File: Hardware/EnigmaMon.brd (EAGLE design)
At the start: 100 x 80 mm, 34 parts, among them T1 BC548, T2 BC548, T3 BC548, T4 BC548, T5 BC548, T6 BC548

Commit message: Added some interesting muxers
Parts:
- removed ARD2: ARD_DIGITAL_1, EnigmaMon:ARD_DIGITAL_1
- removed JP1: (no value), pinhead:2X06
- removed JP2: (no value), pinhead:1X05
- added C2: 10uF, rcl:C025-025X050
- added D8, D9: 1N4004, diode:DO41-10
- added FAN7, FAN8: (no value), pinhead:1X03
- added IC1: 4051N, 40xx:DIL16
- added IC2: TLC5940, EnigmaMon:DIL28-3
- added R15, R17: 1k, rcl:0204/7
- added R16, R18, R_BLANK: 10k, rcl:0204/7
- added R_IREF: 2.2k, rcl:0204/7
- added T8, T9: BC548, transistor:TO92
- added U$1: ARD_POWER, EnigmaMon:ARD_POWER
- added U$2: ARD_DIGITAL_1, EnigmaMon:ARD_DIGITAL_1
- added U$3: ARD_DIGITAL_2, EnigmaMon:ARD_DIGITAL_2
- R1, R4: value (none) -> 10k; device rcl:0204/7 -> rcl:0207/10
- R10, R12, R6, R8: value (none) -> 10k
- R11, R2, R3, R5, R7, R9: value (none) -> 1k
- moved R12 67.3 mm to (71.1, 71.1), turned to 90 degrees
- moved FAN6 60.2 mm to (71.1, 59.7), turned to 270 degrees
- moved R10 57.5 mm to (66.0, 71.1), turned to 90 degrees
- moved FAN5 53.9 mm to (66.0, 59.7), turned to 270 degrees
- moved FAN1 50.9 mm to (45.7, 59.7), turned to 270 degrees
- moved FAN4 49.4 mm to (61.0, 59.7), turned to 270 degrees
- moved R8 48.4 mm to (61.0, 71.1), turned to 90 degrees
- moved FAN2 47.8 mm to (50.8, 59.7), turned to 270 degrees
- moved FAN3 47.3 mm to (55.9, 59.7), turned to 270 degrees
- moved T1 46.6 mm to (41.9, 38.1), turned to 0 degrees
- moved R6 40.4 mm to (55.9, 71.1), turned to 90 degrees
- moved R2 39.7 mm to (41.9, 31.8), turned to 90 degrees
- moved D6 39.4 mm to (73.7, 48.3), turned to 270 degrees
- moved T2 37.0 mm to (48.3, 38.1), turned to 0 degrees
- moved R4 33.3 mm to (50.8, 69.8), turned to 90 degrees
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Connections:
- removed net +5V: JP2.4, R1.2, R10.2, R12.2, R4.2, R6.2, R8.2
- removed net 3.3V: JP2.5
- removed net LCD_DATA: ARD2.3
- new net FAN7_GND: D8.C, FAN7.3, T8.3
- new net FAN7_PWM: IC2.2, R15.1
- new net FAN7_TACHO: FAN7.1, IC1.15, R16.1
- new net FAN8_GND: D9.C, FAN8.3, T9.3
- new net FAN8_PWM: IC2.1, R17.1
- new net FAN8_TACHO: FAN8.1, IC1.1, R18.1
- new net FAN_TACHO: IC1.3, U$3.10
- new net N$10: IC2.20, R_IREF.1
- new net N$8: R15.2, T8.2
- new net N$9: R17.2, T9.2
- new net PWM_BLANK: IC2.23, R_BLANK.2, U$2.4
- new net PWM_GSCLK: IC2.18, U$2.5
- new net PWM_SCLK: IC2.25, U$2.7
- new net PWM_SIN: IC2.26, U$3.8
- new net PWM_VPRG: IC2.27, U$3.9
- new net PWM_XLAT: IC2.24, U$2.6
- new net TACHO_SEL0: IC1.11, U$3.11
- new net TACHO_SEL1: IC1.10, U$3.12
- new net TACHO_SEL2: IC1.9, U$3.13
- new net VCC: C2.1, IC1.16, IC2.19, IC2.21, R1.2, R10.2, R12.2, R16.2, R18.2, R4.2, R6.2, R8.2, R_BLANK.1, U$1.5V
- new net VEE: IC1.7
- net +12V: now also FAN7.2, FAN8.2, U$1.VIN; no longer JP2.1
- net FAN1_PWM: now also IC2.8; no longer JP1.2
- net FAN1_TACHO: now also IC1.12; no longer JP1.1
- net FAN2_PWM: now also IC2.7; no longer JP1.4
- net FAN2_TACHO: now also IC1.5; no longer JP1.3
- net FAN3_PWM: now also IC2.6; no longer JP1.6
- net FAN3_TACHO: now also IC1.13; no longer JP1.5
- net FAN4_PWM: now also IC2.5; no longer JP1.8
- net FAN4_TACHO: now also IC1.4; no longer JP1.7
- net FAN5_PWM: now also IC2.4; no longer JP1.10
- net FAN5_TACHO: now also IC1.14; no longer JP1.9
- net FAN6_PWM: now also IC2.3; no longer JP1.12
- net FAN6_TACHO: now also IC1.2; no longer JP1.11
- net GND: now also C2.2, D8.A, D9.A, IC1.6, IC1.8, IC2.22, R_IREF.2, T8.1, T9.1, U$1.GND@1, U$1.GND@2, U$3.GND; no longer JP2.2, JP2.3
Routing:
- net VCC: track 0.00 -> 227.1 mm
- net GND: track 140.7 -> 331.0 mm, vias 6 -> 0
- net +5V: track 101.6 -> 0.00 mm, vias 7 -> 0
- net PWM_VPRG: track 0.00 -> 72.7 mm
- net PWM_BLANK: track 0.00 -> 72.5 mm, vias 0 -> 2
- net PWM_SIN: track 0.00 -> 67.6 mm
- net FAN8_TACHO: track 0.00 -> 67.1 mm
- net PWM_SCLK: track 0.00 -> 67.1 mm, vias 0 -> 2
- net PWM_XLAT: track 0.00 -> 65.8 mm, vias 0 -> 2
- net FAN6_PWM: track 71.1 -> 11.2 mm
- net FAN_TACHO: track 0.00 -> 56.9 mm
- net FAN5_TACHO: track 93.8 -> 39.9 mm
- net FAN6_TACHO: track 107.2 -> 54.4 mm
- net FAN7_TACHO: track 0.00 -> 52.6 mm
- net PWM_GSCLK: track 0.00 -> 51.1 mm
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
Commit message: Added some interesting muxers
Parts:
- PWR: device EnigmaMon:PIN02-1 -> EnigmaMon:1X02
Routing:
- net GND: track 331.0 -> 332.3 mm
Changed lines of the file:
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@@
 </autorouter>
 <elements>
-<element name="PWR" library="EnigmaMon" package="PIN02-1" value="" x="91.44" y="59.69" rot="R90"/>
+<element name="PWR" library="EnigmaMon" package="1X02" value="" x="91.44" y="59.69" rot="R90"/>
 <element name="FAN1" library="pinhead" package="1X03" value="" x="45.72" y="59.69" rot="R270"/>
 <element name="T1" library="transistor" package="TO92" value="BC548" x="41.91" y="38.1" smashed="yes">
@@
 <wire x1="71.12" y1="59.69" x2="76.2" y2="59.69" width="0.8128" layer="16"/>
 <wire x1="71.12" y1="59.69" x2="81.28" y2="59.69" width="0.8128" layer="16"/>
-<wire x1="81.28" y1="59.69" x2="91.44" y2="59.69" width="0.8128" layer="16"/>
+<wire x1="81.28" y1="59.69" x2="91.44" y2="60.96" width="0.8128" layer="16"/>
 </signal>
 <signal name="GND">
@@
 <wire x1="35.56" y1="49.53" x2="8.89" y2="49.53" width="0.8128" layer="16"/>
 <wire x1="8.89" y1="49.53" x2="8.89" y2="62.23" width="0.8128" layer="16"/>
-<wire x1="91.44" y1="57.15" x2="91.44" y2="43.18" width="0.8128" layer="16"/>
+<wire x1="91.44" y1="58.42" x2="91.44" y2="43.18" width="0.8128" layer="16"/>
 <wire x1="91.44" y1="43.18" x2="90.17" y2="41.91" width="0.8128" layer="16"/>
 <wire x1="90.17" y1="41.91" x2="87.63" y2="41.91" width="0.8128" layer="16"/>

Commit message: Added VMR
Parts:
- added C1, C3: 10uF, rcl:E2,5-6
- added INPUT_PWR: (no value), EnigmaMon:1X02
- added LM7805: (no value), EnigmaMon:78XXL
- added R13, R14: 220, rcl:0204/7
- added U$4: DTS6, EnigmaMon:DTS6
- PWR: device EnigmaMon:1X02 -> EnigmaMon:LED3MM
- moved PWR 72.6 mm to (19.1, 54.6), turned to 270 degrees
- moved R4 5.24 mm to (55.9, 71.1)
- moved D1 5.24 mm to (47.0, 49.5)
- moved D2 5.24 mm to (53.3, 49.5)
- moved D4 5.24 mm to (66.0, 49.5)
- moved FAN2 5.24 mm to (55.9, 61.0)
- moved FAN4 5.24 mm to (66.0, 61.0)
- moved R2 5.24 mm to (47.0, 33.0)
- moved R3 5.24 mm to (53.3, 33.0)
- moved R7 5.24 mm to (66.0, 33.0)
- moved R8 5.24 mm to (66.0, 72.4)
- moved T1 5.24 mm to (47.0, 39.4)
- moved T2 5.24 mm to (53.3, 39.4)
- moved T4 5.24 mm to (66.0, 39.4)
- moved R1 5.24 mm to (50.8, 71.1)
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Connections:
- new net N$12: R14.2, U$4.3, U$4.4
- new net N$7: PWR.K, R13.2
- new net RESET: R14.1, U$1.RESET
- net +12V: now also C1.+, INPUT_PWR.2, LM7805.IN; no longer PWR.2
- net GND: now also C1.-, C3.-, INPUT_PWR.1, LM7805.GND, R13.1, U$4.1, U$4.2; no longer PWR.1
- net VCC: now also C3.+, LM7805.OUT, PWR.A
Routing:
- net GND: track 332.3 -> 363.5 mm
- net VCC: track 227.1 -> 258.1 mm, vias 0 -> 2
- net N$12: track 0.00 -> 25.9 mm
- net +12V: track 98.2 -> 111.9 mm
- net PWM_VPRG: track 72.7 -> 80.3 mm
- net TACHO_SEL2: track 38.1 -> 45.7 mm
- net TACHO_SEL1: track 47.5 -> 55.1 mm
- net TACHO_SEL0: track 47.5 -> 55.1 mm
- net PWM_SCLK: track 67.1 -> 74.7 mm
- net PWM_GSCLK: track 51.1 -> 58.7 mm
- net PWM_XLAT: track 65.8 -> 73.4 mm
- net PWM_SIN: track 67.6 -> 75.2 mm
- net PWM_BLANK: track 72.5 -> 80.1 mm
- net FAN_TACHO: track 56.9 -> 63.1 mm
- net RESET: track 0.00 -> 5.61 mm
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
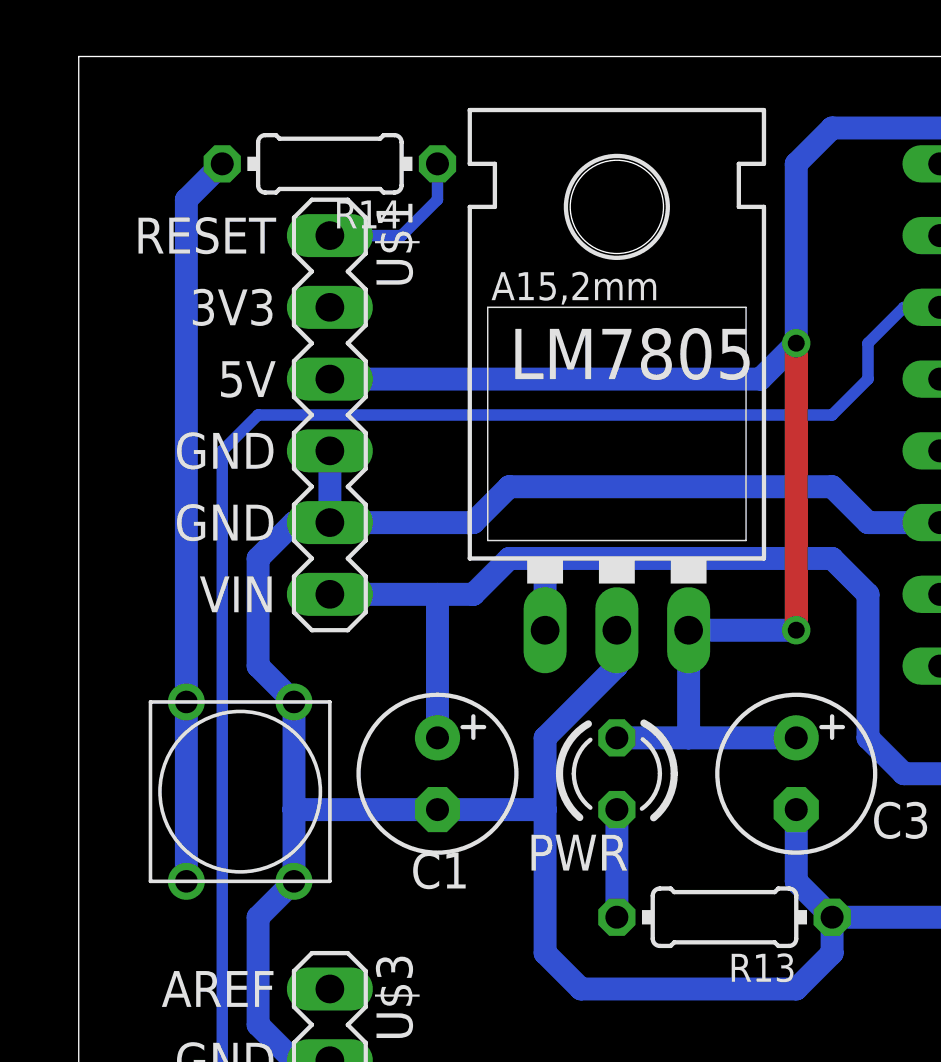
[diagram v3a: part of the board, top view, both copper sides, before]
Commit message: Fixed error with reset switch
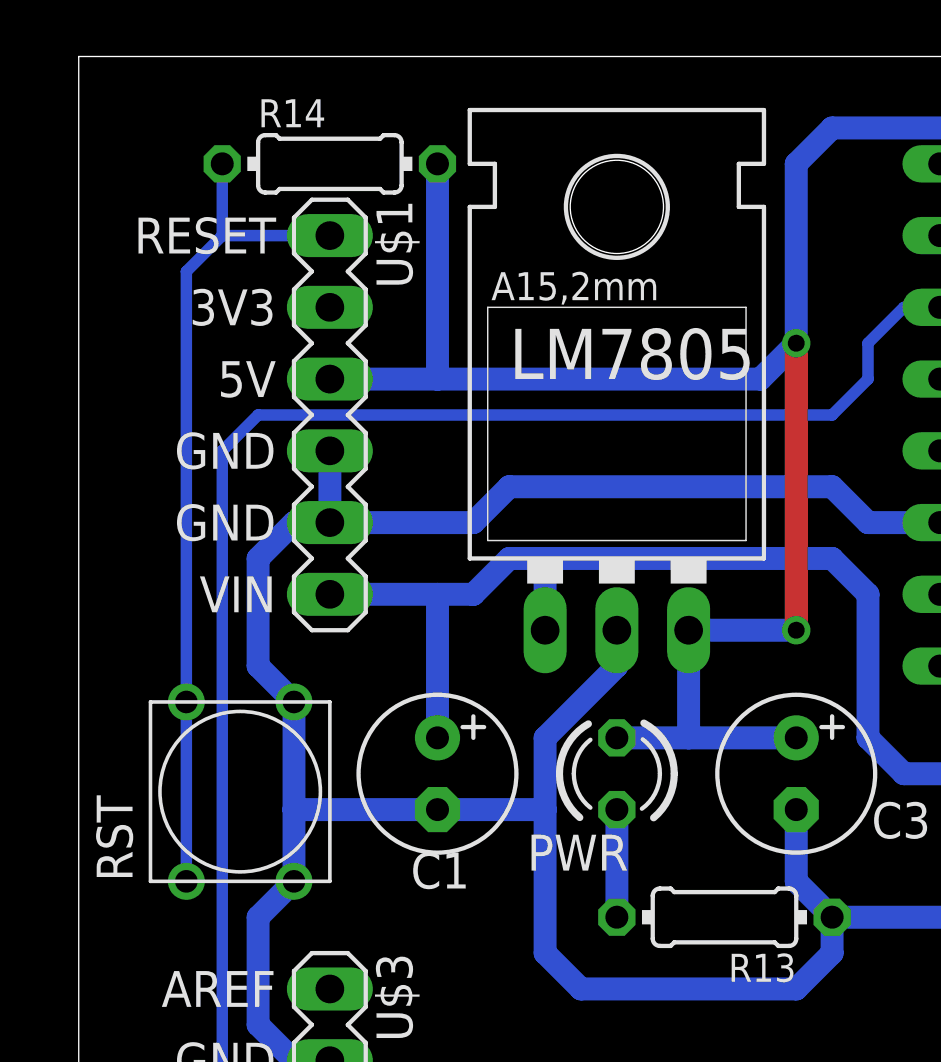
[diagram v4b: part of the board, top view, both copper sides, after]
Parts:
- removed U$4: DTS6, EnigmaMon:DTS6
- added RST: DTS6, EnigmaMon:DTS6
- turned R14 to 0 degrees
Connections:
- removed net N$12: R14.2, U$4.3, U$4.4
- net GND: now also RST.3, RST.4; no longer U$4.1, U$4.2
- net RESET: now also RST.1, RST.2
- net VCC: now also R14.2
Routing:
- net N$12: track 25.9 -> 0.00 mm
- net RESET: track 5.61 -> 29.7 mm
- net VCC: track 258.1 -> 265.7 mm
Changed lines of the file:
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@@
 </element>
 <element name="R13" library="rcl" package="0204/7" value="220" x="22.86" y="49.53" rot="R180"/>
-<element name="R14" library="rcl" package="0204/7" value="220" x="8.89" y="76.2" rot="R180"/>
-<element name="U$4" library="EnigmaMon" package="DTS6" value="DTS6" x="5.08" y="54.61" rot="R270"/>
+<element name="R14" library="rcl" package="0204/7" value="220" x="8.89" y="76.2"/>
+<element name="RST" library="EnigmaMon" package="DTS6" value="DTS6" x="6.35" y="53.34" rot="R90"/>
 </elements>
 <signals>
@@
 <wire x1="16.51" y1="48.26" x2="16.51" y2="53.34" width="0.8128" layer="16"/>
 <wire x1="12.7" y1="53.34" x2="7.62" y2="53.34" width="0.8128" layer="16"/>
-<wire x1="7.62" y1="53.34" x2="7.62" y2="57.15" width="0.8128" layer="16"/>
 <wire x1="7.62" y1="57.15" x2="6.35" y2="58.42" width="0.8128" layer="16"/>
 <wire x1="6.35" y1="58.42" x2="6.35" y2="62.23" width="0.8128" layer="16"/>
@@
 <contactref element="IC2" pad="22"/>
 <wire x1="72.39" y1="7.62" x2="72.39" y2="10.16" width="0.8128" layer="16"/>
-<wire x1="7.62" y1="53.34" x2="7.62" y2="50.8" width="0.8128" layer="16"/>
 <wire x1="7.62" y1="50.8" x2="6.35" y2="49.53" width="0.8128" layer="16"/>
 <wire x1="6.35" y1="49.53" x2="6.35" y2="45.72" width="0.8128" layer="16"/>
@@
 <wire x1="16.51" y1="55.88" x2="16.51" y2="53.34" width="0.8128" layer="16"/>
 <wire x1="16.51" y1="53.34" x2="12.7" y2="53.34" width="0.8128" layer="16"/>
-<contactref element="U$4" pad="1"/>
-<contactref element="U$4" pad="2"/>
+<contactref element="RST" pad="4"/>
+<contactref element="RST" pad="3"/>
+<wire x1="7.62" y1="57.15" x2="7.62" y2="53.34" width="0.8128" layer="16"/>
+<wire x1="7.62" y1="50.8" x2="7.62" y2="53.34" width="0.8128" layer="16"/>
 </signal>
 <signal name="FAN4_TACHO">
@@
 <contactref element="R10" pad="2"/>
 <contactref element="R12" pad="2"/>
-<wire x1="8.89" y1="68.58" x2="24.13" y2="68.58" width="0.8128" layer="16"/>
+<wire x1="8.89" y1="68.58" x2="12.7" y2="68.58" width="0.8128" layer="16"/>
+<wire x1="12.7" y1="68.58" x2="24.13" y2="68.58" width="0.8128" layer="16"/>
 <wire x1="25.4" y1="69.85" x2="25.4" y2="76.2" width="0.8128" layer="16"/>
 <wire x1="25.4" y1="76.2" x2="26.67" y2="77.47" width="0.8128" layer="16"/>
@@
 <via x="25.4" y="69.85" extent="1-16" drill="0.6" shape="square"/>
 <wire x1="25.4" y1="69.85" x2="24.13" y2="68.58" width="0.8128" layer="16"/>
+<contactref element="R14" pad="2"/>
+<wire x1="12.7" y1="76.2" x2="12.7" y2="68.58" width="0.8128" layer="16"/>
+<wire x1="12.7" y1="68.58" x2="8.89" y2="68.58" width="0" layer="19" extent="1-16"/>
 </signal>
 <signal name="TACHO_SEL2">
@@
 <wire x1="19.05" y1="53.34" x2="19.05" y2="49.53" width="0.8128" layer="16"/>
 </signal>
-<signal name="N$12">
-<contactref element="R14" pad="2"/>
-<contactref element="U$4" pad="3"/>
-<contactref element="U$4" pad="4"/>
-<wire x1="3.81" y1="50.8" x2="3.81" y2="57.15" width="0.8128" layer="16"/>
-<wire x1="3.81" y1="57.15" x2="3.81" y2="74.93" width="0.8128" layer="16"/>
-<wire x1="3.81" y1="74.93" x2="5.08" y2="76.2" width="0.8128" layer="16"/>
-</signal>
 <signal name="RESET">
 <contactref element="R14" pad="1"/>
 <contactref element="U$1" pad="RESET"/>
-<wire x1="12.7" y1="76.2" x2="12.7" y2="74.93" width="0.4064" layer="16"/>
-<wire x1="12.7" y1="74.93" x2="11.43" y2="73.66" width="0.4064" layer="16"/>
-<wire x1="11.43" y1="73.66" x2="8.89" y2="73.66" width="0.4064" layer="16"/>
+<wire x1="5.08" y1="76.2" x2="5.08" y2="73.66" width="0.4064" layer="16"/>
+<contactref element="RST" pad="1"/>
+<contactref element="RST" pad="2"/>
+<wire x1="3.81" y1="57.15" x2="3.81" y2="72.39" width="0.4064" layer="16"/>
+<wire x1="3.81" y1="72.39" x2="5.08" y2="73.66" width="0.4064" layer="16"/>
+<wire x1="5.08" y1="73.66" x2="8.89" y2="73.66" width="0.4064" layer="16"/>
+<wire x1="3.81" y1="57.15" x2="3.81" y2="50.8" width="0.4064" layer="16"/>
 </signal>
 </signals>

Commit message: Couple of minor updates
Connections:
- net GND: now also IC2.10, IC2.11, IC2.12, IC2.13, IC2.14, IC2.15, IC2.9
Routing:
- net GND: track 363.5 -> 394.5 mm
- net PWM_SIN: track 75.2 -> 89.0 mm
- net PWM_VPRG: track 80.3 -> 94.1 mm
- net PWM_XLAT: track 73.4 -> 77.0 mm
- net PWM_SCLK: track 74.7 -> 78.3 mm
- net PWM_GSCLK: track 58.7 -> 61.3 mm
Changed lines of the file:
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@@
 <wire x1="7.62" y1="57.15" x2="7.62" y2="53.34" width="0.8128" layer="16"/>
 <wire x1="7.62" y1="50.8" x2="7.62" y2="53.34" width="0.8128" layer="16"/>
+<contactref element="IC2" pad="9"/>
+<contactref element="IC2" pad="10"/>
+<contactref element="IC2" pad="11"/>
+<contactref element="IC2" pad="12"/>
+<contactref element="IC2" pad="13"/>
+<contactref element="IC2" pad="14"/>
+<contactref element="IC2" pad="15"/>
+<wire x1="44.45" y1="22.86" x2="43.18" y2="24.13" width="0.8128" layer="16"/>
+<wire x1="43.18" y1="24.13" x2="43.18" y2="33.02" width="0.8128" layer="16"/>
+<wire x1="44.45" y1="22.86" x2="46.99" y2="22.86" width="0.8128" layer="16"/>
+<wire x1="46.99" y1="22.86" x2="49.53" y2="22.86" width="0.8128" layer="16"/>
+<wire x1="49.53" y1="22.86" x2="52.07" y2="22.86" width="0.8128" layer="16"/>
+<wire x1="52.07" y1="22.86" x2="54.61" y2="22.86" width="0.8128" layer="16"/>
+<wire x1="54.61" y1="22.86" x2="57.15" y2="22.86" width="0.8128" layer="16"/>
+<wire x1="44.45" y1="22.86" x2="44.45" y2="15.24" width="0.8128" layer="16"/>
 </signal>
 <signal name="FAN4_TACHO">
@@
 <wire x1="8.89" y1="20.32" x2="22.86" y2="20.32" width="0.4064" layer="16"/>
 <wire x1="22.86" y1="20.32" x2="24.13" y2="19.05" width="0.4064" layer="16"/>
-<wire x1="24.13" y1="19.05" x2="24.13" y2="10.16" width="0.4064" layer="16"/>
-<wire x1="24.13" y1="10.16" x2="25.4" y2="8.89" width="0.4064" layer="16"/>
-<wire x1="25.4" y1="8.89" x2="50.8" y2="8.89" width="0.4064" layer="16"/>
-<wire x1="50.8" y1="8.89" x2="52.07" y2="10.16" width="0.4064" layer="16"/>
-<wire x1="52.07" y1="10.16" x2="52.07" y2="15.24" width="0.4064" layer="16"/>
+<wire x1="24.13" y1="19.05" x2="24.13" y2="8.89" width="0.4064" layer="16"/>
+<wire x1="24.13" y1="8.89" x2="25.4" y2="7.62" width="0.4064" layer="16"/>
+<wire x1="25.4" y1="7.62" x2="50.8" y2="7.62" width="0.4064" layer="16"/>
+<wire x1="50.8" y1="7.62" x2="52.07" y2="8.89" width="0.4064" layer="16"/>
+<wire x1="52.07" y1="8.89" x2="52.07" y2="15.24" width="0.4064" layer="16"/>
 </signal>
 <signal name="PWM_XLAT">
@@
 <wire x1="67.31" y1="15.24" x2="67.31" y2="11.43" width="0.4064" layer="16"/>
 <via x="67.31" y="11.43" extent="1-16" drill="0.6" shape="square"/>
-<wire x1="67.31" y1="11.43" x2="50.8" y2="11.43" width="0.4064" layer="1"/>
-<via x="50.8" y="11.43" extent="1-16" drill="0.6" shape="square"/>
-<wire x1="50.8" y1="11.43" x2="26.67" y2="11.43" width="0.4064" layer="16"/>
-<wire x1="26.67" y1="11.43" x2="25.4" y2="12.7" width="0.4064" layer="16"/>
-<wire x1="25.4" y1="12.7" x2="25.4" y2="21.59" width="0.4064" layer="16"/>
+<wire x1="67.31" y1="11.43" x2="55.88" y2="11.43" width="0.4064" layer="1"/>
+<wire x1="55.88" y1="11.43" x2="53.34" y2="8.89" width="0.4064" layer="1"/>
+<wire x1="53.34" y1="8.89" x2="49.53" y2="8.89" width="0.4064" layer="1"/>
+<via x="49.53" y="8.89" extent="1-16" drill="0.6" shape="square"/>
+<wire x1="49.53" y1="8.89" x2="26.67" y2="8.89" width="0.4064" layer="16"/>
+<wire x1="26.67" y1="8.89" x2="25.4" y2="10.16" width="0.4064" layer="16"/>
+<wire x1="25.4" y1="10.16" x2="25.4" y2="21.59" width="0.4064" layer="16"/>
 <wire x1="25.4" y1="21.59" x2="24.13" y2="22.86" width="0.4064" layer="16"/>
 <wire x1="24.13" y1="22.86" x2="8.89" y2="22.86" width="0.4064" layer="16"/>
@@
 <contactref element="IC2" pad="25"/>
 <contactref element="U$2" pad="7"/>
-<wire x1="50.8" y1="12.7" x2="27.94" y2="12.7" width="0.4064" layer="16"/>
-<wire x1="27.94" y1="12.7" x2="26.67" y2="13.97" width="0.4064" layer="16"/>
-<wire x1="26.67" y1="13.97" x2="26.67" y2="24.13" width="0.4064" layer="16"/>
+<wire x1="49.53" y1="10.16" x2="27.94" y2="10.16" width="0.4064" layer="16"/>
+<wire x1="27.94" y1="10.16" x2="26.67" y2="11.43" width="0.4064" layer="16"/>
+<wire x1="26.67" y1="11.43" x2="26.67" y2="24.13" width="0.4064" layer="16"/>
 <wire x1="26.67" y1="24.13" x2="25.4" y2="25.4" width="0.4064" layer="16"/>
 <wire x1="25.4" y1="25.4" x2="8.89" y2="25.4" width="0.4064" layer="16"/>
 <wire x1="69.85" y1="15.24" x2="69.85" y2="12.7" width="0.4064" layer="16"/>
 <via x="69.85" y="12.7" extent="1-16" drill="0.6" shape="square"/>
-<wire x1="69.85" y1="12.7" x2="50.8" y2="12.7" width="0.4064" layer="1"/>
-<via x="50.8" y="12.7" extent="1-16" drill="0.6" shape="square"/>
+<wire x1="69.85" y1="12.7" x2="55.88" y2="12.7" width="0.4064" layer="1"/>
+<wire x1="55.88" y1="12.7" x2="53.34" y2="10.16" width="0.4064" layer="1"/>
+<wire x1="53.34" y1="10.16" x2="49.53" y2="10.16" width="0.4064" layer="1"/>
+<via x="49.53" y="10.16" extent="1-16" drill="0.6" shape="square"/>
 </signal>
 <signal name="PWM_SIN">
@@
 <wire x1="8.89" y1="29.21" x2="26.67" y2="29.21" width="0.4064" layer="16"/>
 <wire x1="26.67" y1="29.21" x2="27.94" y2="27.94" width="0.4064" layer="16"/>
-<wire x1="27.94" y1="27.94" x2="27.94" y2="20.32" width="0.4064" layer="16"/>
-<wire x1="27.94" y1="20.32" x2="29.21" y2="19.05" width="0.4064" layer="16"/>
-<wire x1="29.21" y1="19.05" x2="71.12" y2="19.05" width="0.4064" layer="16"/>
+<wire x1="27.94" y1="27.94" x2="27.94" y2="12.7" width="0.4064" layer="16"/>
+<wire x1="27.94" y1="12.7" x2="29.21" y2="11.43" width="0.4064" layer="16"/>
+<wire x1="29.21" y1="11.43" x2="49.53" y2="11.43" width="0.4064" layer="16"/>
+<wire x1="49.53" y1="11.43" x2="50.8" y2="12.7" width="0.4064" layer="16"/>
+<wire x1="50.8" y1="12.7" x2="50.8" y2="17.78" width="0.4064" layer="16"/>
+<wire x1="50.8" y1="17.78" x2="52.07" y2="19.05" width="0.4064" layer="16"/>
+<wire x1="52.07" y1="19.05" x2="71.12" y2="19.05" width="0.4064" layer="16"/>
 <wire x1="71.12" y1="19.05" x2="72.39" y2="17.78" width="0.4064" layer="16"/>
 <wire x1="72.39" y1="17.78" x2="72.39" y2="15.24" width="0.4064" layer="16"/>
@@
 <wire x1="8.89" y1="31.75" x2="27.94" y2="31.75" width="0.4064" layer="16"/>
 <wire x1="27.94" y1="31.75" x2="29.21" y2="30.48" width="0.4064" layer="16"/>
-<wire x1="29.21" y1="30.48" x2="29.21" y2="21.59" width="0.4064" layer="16"/>
-<wire x1="29.21" y1="21.59" x2="30.48" y2="20.32" width="0.4064" layer="16"/>
-<wire x1="30.48" y1="20.32" x2="73.66" y2="20.32" width="0.4064" layer="16"/>
+<wire x1="29.21" y1="30.48" x2="29.21" y2="13.97" width="0.4064" layer="16"/>
+<wire x1="29.21" y1="13.97" x2="30.48" y2="12.7" width="0.4064" layer="16"/>
+<wire x1="30.48" y1="12.7" x2="46.99" y2="12.7" width="0.4064" layer="16"/>
+<wire x1="46.99" y1="12.7" x2="48.26" y2="13.97" width="0.4064" layer="16"/>
+<wire x1="48.26" y1="13.97" x2="48.26" y2="19.05" width="0.4064" layer="16"/>
+<wire x1="48.26" y1="19.05" x2="49.53" y2="20.32" width="0.4064" layer="16"/>
+<wire x1="49.53" y1="20.32" x2="73.66" y2="20.32" width="0.4064" layer="16"/>
 <wire x1="73.66" y1="20.32" x2="74.93" y2="19.05" width="0.4064" layer="16"/>
 <wire x1="74.93" y1="19.05" x2="74.93" y2="15.24" width="0.4064" layer="16"/>
